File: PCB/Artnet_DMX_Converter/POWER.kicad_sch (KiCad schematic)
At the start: 18 parts, among them IC1 NPM1300-QEAA-R7

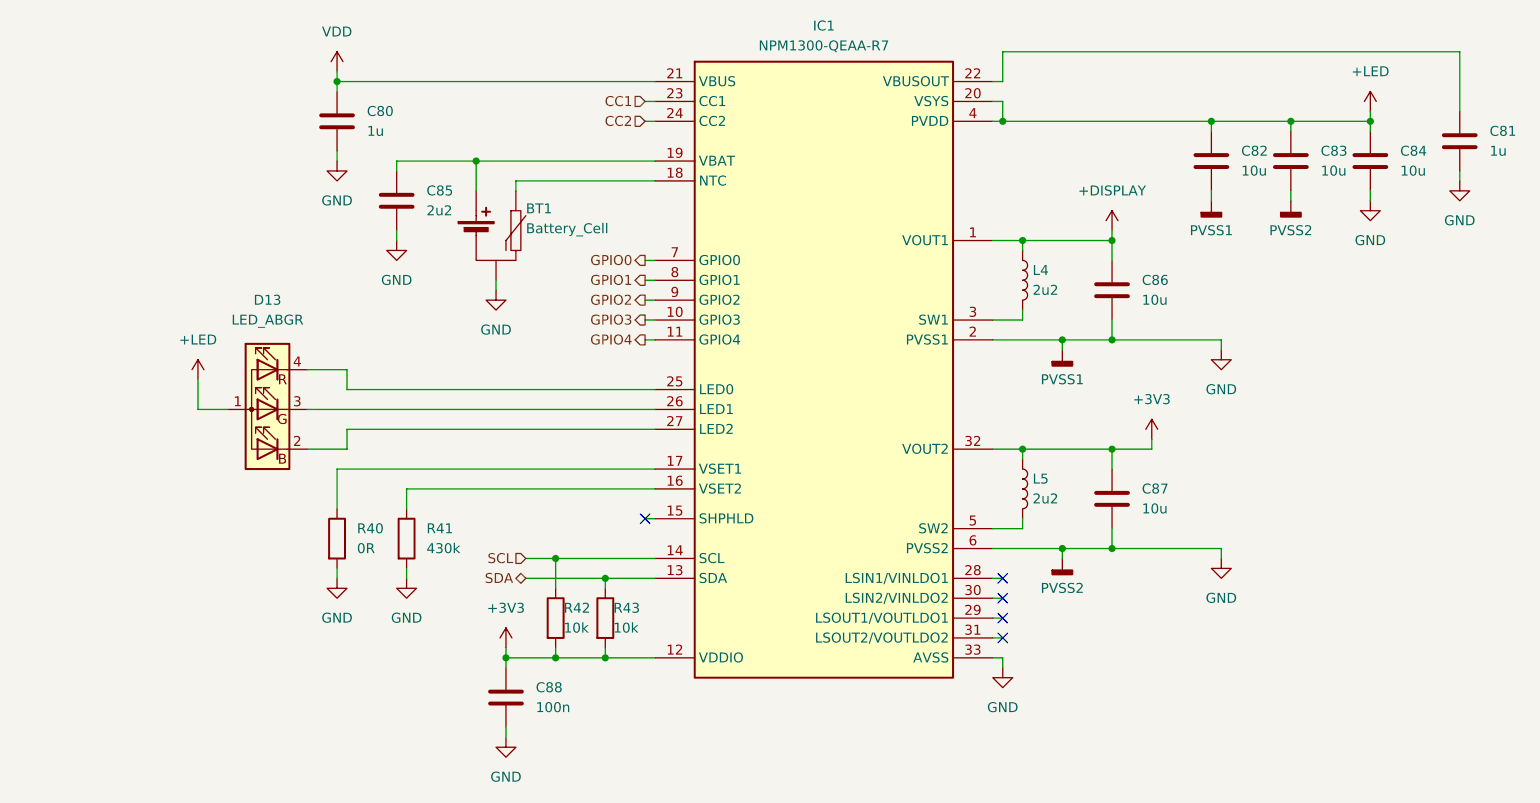
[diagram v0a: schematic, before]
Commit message: Updated the PCB Allot
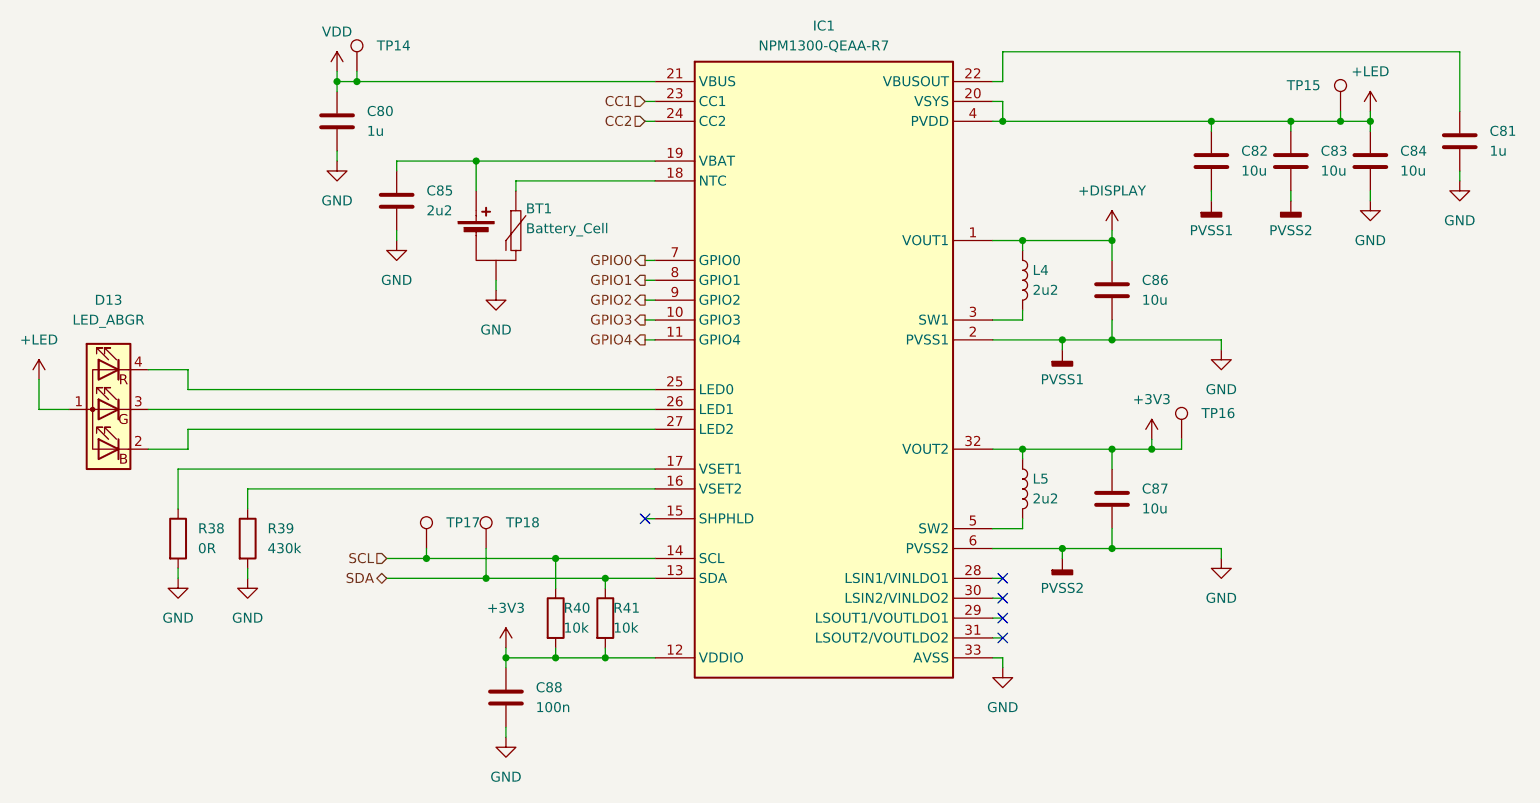
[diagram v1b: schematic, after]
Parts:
- added TP14, TP15, TP16, TP17, TP18: TestPoint, TestPoint:TestPoint_Pad_D1.5mm, symbol Connector:TestPoint
- renumbered R40 to R38, R41 to R39, R42 to R40, R43 to R41
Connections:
- net +3V3: now also TP16.1
- net +LED: now also TP15.1
- net SCL: now also TP17.1
- net SDA: now also TP18.1
- net VDD: now also TP14.1
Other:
- moved on the sheet: D13, R38, R39
